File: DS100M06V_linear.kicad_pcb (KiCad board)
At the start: 4 copper layers, 110 x 52 mm, 108 parts, among them J1 wire2board, J10 BNC_panel_mount, J11 wire2board, J2 Wire2Board, J3 wire2board, J4 wire2board, J5 Wire2Board, J6 Wire2Board, J7 Wire2Board, J8 red_safety_4mm_connector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

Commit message: Back to linear.
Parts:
- removed L2, L3: 4.7u, Inductor_SMD:L_Bourns_SRN6045TA
- added C3: 1u, Resistor_SMD:R_0603_1608Metric_Pad0.98x0.95mm_HandSolder, F.Cu at (170.7, 111.0)
- added PS1: IA0509S, Converter_DCDC:Converter_DCDC_XP_POWER-IAxxxxS_THT, F.Cu at (192.9, 125.8)
- added U3: L7905, Package_TO_SOT_THT:TO-220-3_Horizontal_TabDown, F.Cu at (175.2, 111.9)
- SW1: footprint Button_Switch_THT:SW_CuK_JS202011CQN_DPDT_Straight -> Button_Switch_THT:SW_CK_JS202011CQN_DPDT_Straight
- U6: value TEA1-0505 -> L7805; footprint Converter_DCDC:Converter_DCDC_TRACO_TEA1-xxxx_THT -> Package_TO_SOT_THT:TO-220-3_Horizontal_TabDown
- moved RV5 52.7 mm to (128.8, 146.8), turned to 0 degrees
- moved Q2 48.1 mm to (144.3, 143.5), turned to 180 degrees
- moved U5 45.7 mm to (143.7, 139.6)
- moved C12 45.3 mm to (93.8, 114.5), turned to 180 degrees
- moved R29 45.2 mm to (139.4, 140.7)
- moved C13 43.9 mm to (99.0, 114.5), turned to 180 degrees
- moved R14 43.5 mm to (120.9, 109.5), turned to 90 degrees
- moved C14 42.7 mm to (104.2, 114.5), turned to 180 degrees
- moved D5 41.8 mm to (124.7, 109.2), turned to 90 degrees
- moved C15 41.5 mm to (109.4, 114.5), turned to 180 degrees
- moved U2 40.8 mm to (153.7, 144.4), turned to 180 degrees
- moved D4 40.1 mm to (122.7, 109.2), turned to 90 degrees
- moved C2 39.8 mm to (146.8, 139.7), turned to 90 degrees
- moved C8 35.8 mm to (122.6, 113.0)
- moved R30 35.7 mm to (148.4, 139.7), turned to -90 degrees
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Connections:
- C1 pad 2: 0 -> Earth
- C16 pad 1: 0 -> Earth
- C17 pad 1: 0 -> Earth
- C17 pad 2: Net-(U6-+Vin) -> Net-(PS1-+Vin)
- C2 pad 2: 0 -> Earth
- C28 pad 1: Net-(U6-+Vin) -> Net-(PS1-+Vin)
- C28 pad 2: 0 -> Earth
- C29 pad 1: Net-(U6--Vout) -> Net-(PS1--Vout)
- J5 pad 1: 0 -> Earth
- Q2 pad 1: (no net) -> unconnected-(Q2-D-Pad1)
- Q2 pad 2: (no net) -> Earth
- Q2 pad 3: (no net) -> Earth
- Q2 pad 6: (no net) -> -BAT
- Q2 pad 7: (no net) -> -BAT
- Q2 pad 8: (no net) -> unconnected-(Q2-D-Pad8)
- R25 pad 1: 0 -> Earth
- R26 pad 1: 0 -> Earth
- R27 pad 1: 0 -> Earth
- R28 pad 2: Net-(U6-+Vin) -> Net-(PS1-+Vin)
- U2 pad 3: 0 -> Earth
- U2 pad 9: 0 -> Earth
- U5 pad 6: 0 -> Earth
- U6 pad 1: 0 -> Net-(PS1-+Vout)
- U6 pad 2: Net-(U6-+Vin) -> 0
- U6 pad 3: Net-(U6--Vout) -> +5V
- U7 pad 2: 0 -> Earth
- U7 pad 5: Net-(U6-+Vin) -> Net-(PS1-+Vin)
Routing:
- net 0: track 80.0 -> 30.4 mm
- net (no net): track 41.0 -> 0.00 mm
- net +5V: track 61.1 -> 41.3 mm
- net Net-(C15-Pad1): track 23.4 -> 4.26 mm
- net Net-(C11-Pad1): track 28.0 -> 8.89 mm
- net Net-(U6-+Vin): track 12.0 -> 0.00 mm
- net -5V: track 25.7 -> 17.5 mm
- net Net-(R12-Pad1): track 4.90 -> 0.00 mm
- net Net-(R5-Pad1): track 4.42 -> 0.00 mm
- net Net-(C12-Pad1): track 0.00 -> 3.46 mm
- net Net-(C14-Pad1): track 0.00 -> 3.38 mm
- net Net-(C13-Pad1): track 0.00 -> 3.38 mm
- net Net-(U1B-+): track 9.59 -> 6.31 mm
- net Net-(U1A-+): track 10.1 -> 6.83 mm
- net IN-: track 6.09 -> 5.37 mm

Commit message: Ill flip ya for it.
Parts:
- added H5: WireFeedHole, MountingHole:MountingHole_2.2mm_M2_ISO7380, F.Cu at (94.0, 109.0)
- added H6: WireFeedHole, MountingHole:MountingHole_2.2mm_M2_ISO7380, F.Cu at (89.0, 112.0)
- added H7: WireFeedHole, MountingHole:MountingHole_2.2mm_M2_ISO7380, F.Cu at (93.0, 140.0)
- added H8: WireFeedHole, MountingHole:MountingHole_2.2mm_M2_ISO7380, F.Cu at (89.0, 137.0)
- J10, J8, PS1, RV1, RV2, RV3, RV4, RV5, RV6: moved to B.Cu
- J9: footprint DS100M06V_linear:black_safety_4mm_connector -> DS100M06V_linear:red_safety_4mm_connector; moved to B.Cu
- moved C28 8.33 mm to (192.3, 120.4)
- moved RV6 7.40 mm to (115.8, 102.5), turned to 180 degrees
- moved RV2 5.91 mm to (126.7, 126.0), turned to 0 degrees
- moved RV1 5.65 mm to (112.9, 147.0), turned to 180 degrees
- moved RV5 5.05 mm to (123.8, 146.9), turned to 180 degrees
- moved RV3 4.69 mm to (129.3, 101.9), turned to 180 degrees
- moved J10 3.22 mm to (196.9, 136.9)
- moved C10 3.00 mm to (104.2, 133.0)
- moved C11 3.00 mm to (109.4, 133.0)
- moved C39 3.00 mm to (93.7, 133.0)
- moved C9 3.00 mm to (99.0, 133.0)
- moved J3 3.00 mm to (89.5, 133.1)
- moved R1 3.00 mm to (99.0, 135.5)
- moved R2 3.00 mm to (104.2, 135.5)
- moved R3 3.00 mm to (109.4, 135.5)
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
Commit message: Veći prekidač.
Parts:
- SW1: footprint Button_Switch_THT:SW_CK_JS202011CQN_DPDT_Straight -> DS100M06V_linear:DPDT_bigger
- moved C17 5.90 mm to (166.0, 138.0)
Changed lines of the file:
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@@
 	(footprint "Resistor_SMD:R_0603_1608Metric_Pad0.98x0.95mm_HandSolder"
 		(layer "F.Cu")
-		(at 166.2 143.9 180)
+		(at 166 138 180)
 		(descr "Resistor SMD 0603 (1608 Metric), square (rectangular) end terminal, IPC_7351 nominal with elongated pad for handsoldering. (Body size source: IPC-SM-782 page 72, https://www.pcb-3d.com/wordpress/wp-content/uploads/ipc-sm-782a_amendment_1_and_2.pdf), generated with kicad-footprint-generator")
 		(tags "resistor handsolder")
@@
 		)
 	)
-	(footprint "Button_Switch_THT:SW_CK_JS202011CQN_DPDT_Straight"
+	(footprint "DS100M06V_linear:DPDT_bigger"
 		(layer "F.Cu")
 		(at 139 121.3575)
@@
 			)
 		)
-		(property "Footprint" "Button_Switch_THT:SW_CK_JS202011CQN_DPDT_Straight"
+		(property "Footprint" "DS100M06V_linear:DPDT_bigger"
 			(at 0 0 0)
 			(unlocked yes)
@@
 		)
 		(fp_line
-			(start -2.25 -0.95)
-			(end 7.25 -0.95)
+			(start -2.25 4.3)
+			(end -2.25 -0.95)
 			(stroke
 				(width 0.05)
@@
 		)
 		(fp_line
-			(start -2.25 4.25)
-			(end -2.25 -0.95)
+			(start -1.75 -1)
+			(end 10.7 -1)
 			(stroke
 				(width 0.05)
@@
 		)
 		(fp_line
-			(start 7.25 -0.95)
-			(end 7.25 4.25)
+			(start 10.7 -1)
+			(end 10.7 4.3)
 			(stroke
 				(width 0.05)
@@
 		)
 		(fp_line
-			(start 7.25 4.25)
-			(end -2.25 4.25)
+			(start 10.7 4.3)
+			(end -2.25 4.3)
 			(stroke
 				(width 0.05)
@@
 			)
 		)
-		(pad "1" thru_hole roundrect
-			(at 0 0)
-			(size 1.4 1.4)
-			(drill 0.9)
+		(pad "1" thru_hole oval
+			(at 0 0.1)
+			(size 2.7 1.5)
+			(drill oval 2.2 1)
 			(layers "*.Cu" "*.Mask")
 			(remove_unused_layers no)
-			(roundrect_rratio 0.1785714286)
 			(net 23 "Net-(SW1A-A)")
 			(pinfunction "A")
 			(pintype "passive")
 		)
-		(pad "2" thru_hole circle
-			(at 2.5 0)
-			(size 1.4 1.4)
-			(drill 0.9)
+		(pad "2" thru_hole oval
+			(at 4 0.1)
+			(size 2.7 1.5)
+			(drill oval 2.2 1)
 			(layers "*.Cu" "*.Mask")
 			(remove_unused_layers no)
@@
 			(pintype "passive")
 		)
-		(pad "3" thru_hole circle
-			(at 5 0)
-			(size 1.4 1.4)
-			(drill 0.9)
+		(pad "3" thru_hole oval
+			(at 8 0.1)
+			(size 2.7 1.5)
+			(drill oval 2.2 1)
 			(layers "*.Cu" "*.Mask")
 			(remove_unused_layers no)
@@
 			(pintype "passive")
 		)
-		(pad "4" thru_hole circle
-			(at 5 3.3)
-			(size 1.4 1.4)
-			(drill 0.9)
+		(pad "4" thru_hole oval
+			(at 8 3.2)
+			(size 2.7 1.5)
+			(drill oval 2.2 1)
 			(layers "*.Cu" "*.Mask")
 			(remove_unused_layers no)
@@
 			(pintype "passive")
 		)
-		(pad "5" thru_hole circle
-			(at 2.5 3.3)
-			(size 1.4 1.4)
-			(drill 0.9)
+		(pad "5" thru_hole oval
+			(at 4 3.2)
+			(size 2.7 1.5)
+			(drill oval 2.2 1)
 			(layers "*.Cu" "*.Mask")
 			(remove_unused_layers no)
@@
 			(pintype "passive")
 		)
-		(pad "6" thru_hole circle
-			(at 0 3.3)
-			(size 1.4 1.4)
-			(drill 0.9)
+		(pad "6" thru_hole oval
+			(at 0 3.2)
+			(size 2.7 1.5)
+			(drill oval 2.2 1)
 			(layers "*.Cu" "*.Mask")
 			(remove_unused_layers no)
@@
 			(pintype "passive")
 		)
-		(model "${KICAD8_3DMODEL_DIR}/Button_Switch_THT.3dshapes/SW_CK_JS202011CQN_DPDT_Straight.wrl"
+		(model "${DS100M06V}/DPDT Slide Switch.step"
 			(offset
-				(xyz 0 0 0)
+				(xyz -7 -1.6 8)
 			)
 			(scale
@@
 		(tags "cliff 4mm socket jack banana green")
 		(property "Reference" "J9"
-			(at 0 10.25 360)
+			(at 0 10.25 0)
 			(layer "B.SilkS")
 			(effects
@@
 		)
 		(property "Value" "black_safety_4mm_connector"
-			(at 0 -9.75 360)
+			(at 0 -9.75 0)
 			(layer "B.Fab")
 			(effects
@@
 		)
 		(fp_text user "${REFERENCE}"
-			(at 0 0 360)
+			(at 0 0 0)
 			(layer "B.Fab")
 			(effects
@@
 		(tags "cliff 4mm socket jack banana green")
 		(property "Reference" "J10"
-			(at 0 10.25 360)
+			(at 0 10.25 0)
 			(layer "B.SilkS")
 			(effects
@@
 		)
 		(property "Value" "BNC_panel_mount"
-			(at 0 -9.75 360)
+			(at 0 -9.75 0)
 			(layer "B.Fab")
 			(effects
@@
 		)
 		(fp_text user "${REFERENCE}"
-			(at 0 0 360)
+			(at 0 0 0)
 			(layer "B.Fab")
 			(effects
@@
 		(tags "cliff 4mm socket jack banana green")
 		(property "Reference" "J8"
-			(at 0 10.25 360)
+			(at 0 10.25 0)
 			(layer "B.SilkS")
 			(effects
@@
 		)
 		(property "Value" "red_safety_4mm_connector"
-			(at 0 -9.75 360)
+			(at 0 -9.75 0)
 			(layer "B.Fab")
 			(effects
@@
 		)
 		(fp_text user "${REFERENCE}"
-			(at 0 0 360)
+			(at 0 0 0)
 			(layer "B.Fab")
 			(effects

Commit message: Img tst
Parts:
- removed C16: 1n, Resistor_SMD:R_0603_1608Metric_Pad0.98x0.95mm_HandSolder
- removed RV3: 100, Potentiometer_THT:Potentiometer_Bourns_3296W_Vertical
- added C19: 1u, Resistor_SMD:R_0603_1608Metric_Pad0.98x0.95mm_HandSolder, F.Cu at (116.5, 120.2)
- added C33: 100n, Resistor_SMD:R_0603_1608Metric_Pad0.98x0.95mm_HandSolder, F.Cu at (116.5, 118.7)
- added C34: 1n, Resistor_SMD:R_0603_1608Metric_Pad0.98x0.95mm_HandSolder, F.Cu at (116.5, 117.2)
- added C36: 470u, Capacitor_THT:CP_Radial_D8.0mm_P3.50mm, B.Cu at (166.7, 134.5)
- added C4: 100n, Resistor_SMD:R_0603_1608Metric_Pad0.98x0.95mm_HandSolder, F.Cu at (145.4, 129.2)
- added C40: 470u, Capacitor_THT:CP_Radial_D8.0mm_P3.50mm, B.Cu at (168.6, 143.3)
- added C41: 10u, Resistor_SMD:R_1206_3216Metric_Pad1.30x1.75mm_HandSolder, F.Cu at (161.8, 146.8)
- added C42: 10u, Resistor_SMD:R_1206_3216Metric_Pad1.30x1.75mm_HandSolder, F.Cu at (161.8, 144.5)
- added C43: 10u, Resistor_SMD:R_1206_3216Metric_Pad1.30x1.75mm_HandSolder, F.Cu at (153.7, 145.8)
- added L2: 4.7u, Inductor_THT:L_Radial_D7.5mm_P3.50mm_Fastron_07P, B.Cu at (159.2, 139.8)
- added SW2: SW_DPDT_x2, DS100M06V_linear:DPDT_bigger, F.Cu at (136.5, 134.4)
- C17, C26: value 1n -> 1u
- C18, C21: value 1u -> 100n
- C20: value 1n -> 470u; footprint Resistor_SMD:R_0603_1608Metric_Pad0.98x0.95mm_HandSolder -> Capacitor_THT:CP_Radial_D8.0mm_P3.50mm; moved to B.Cu
- C35, C37: value 1u -> 1n
- moved C7 52.3 mm to (112.7, 133.0), turned to 90 degrees
- moved C6 51.7 mm to (115.9, 133.0), turned to 90 degrees
- moved C5 50.1 mm to (115.9, 114.7)
- moved TP3 37.6 mm to (166.7, 131.3)
- moved C20 36.3 mm to (166.6, 113.9), turned to -90 degrees
- moved J5 33.2 mm to (131.9, 146.0), turned to -90 degrees
- moved R23 29.2 mm to (114.0, 118.1), turned to -90 degrees
- moved TP4 28.4 mm to (166.5, 110.4)
- moved J2 26.4 mm to (135.7, 146.0), turned to -90 degrees
- moved R24 24.0 mm to (142.4, 122.0), turned to 0 degrees
- moved C3 23.2 mm to (169.6, 134.2), turned to -90 degrees
- moved C27 22.2 mm to (126.3, 125.4), turned to 180 degrees
- moved J10 21.8 mm to (190.9, 115.9)
- moved C25 20.8 mm to (148.8, 121.0)
- moved RV4 19.2 mm to (148.4, 125.8), turned to 0 degrees
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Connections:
- C20 pad 1: 0 -> -5V
- C20 pad 2: +5V -> 0
- L1 pad 1: +BAT -> Net-(SW2A-B)
- RV2 pad 1: 0 -> Net-(R12-Pad1)
- TP3 pad 1: -5V -> +5V
- U7 pad 3: +BAT -> Net-(SW2A-B)
- U7 pad 6: +BAT -> Net-(SW2A-B)
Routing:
- net +5V: track 41.4 -> 5.34 mm
- net 0: track 30.4 -> 6.45 mm
- net -5V: track 17.3 -> 1.48 mm
- net Net-(C15-Pad1): track 4.26 -> 17.2 mm
- net Net-(SW1B-A): track 7.35 -> 14.8 mm
- net Net-(C32-Pad2): track 6.70 -> 0.00 mm
- net Net-(SW1B-C): track 11.7 -> 5.05 mm
- net Net-(U1A-+): track 6.83 -> 13.4 mm
- net Net-(D4-K): track 0.00 -> 5.57 mm
- net Net-(J1-Pin_1): track 4.73 -> 0.00 mm
- net Net-(U4--): track 12.8 -> 8.67 mm
- net Net-(C11-Pad1): track 8.89 -> 12.3 mm
- net Net-(SW1A-C): track 11.0 -> 14.3 mm
- net Net-(U1B-+): track 6.31 -> 9.43 mm
- net Net-(SW1A-B): track 12.9 -> 14.8 mm
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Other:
- board text removed: "+"
- board text removed: "-"
- board text removed: "-5V"
- board text removed: "G"

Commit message: Layout skoro gotov.
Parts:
- C27: value 1n -> 1u
- moved J6 15.2 mm to (130.8, 138.9)
- moved C43 10.7 mm to (155.6, 135.3), turned to 0 degrees
- moved R29 7.43 mm to (136.8, 144.7)
- moved D7 3.63 mm to (120.3, 123.0), turned to 0 degrees
- moved H2 3.40 mm to (180.0, 104.9)
- moved H4 3.40 mm to (180.0, 144.9)
- moved J5 2.64 mm to (134.3, 147.1)
- moved C20 2.60 mm to (166.7, 116.5)
- moved PS1 2.45 mm to (189.6, 125.4)
- moved C18 2.43 mm to (123.9, 123.6)
- moved C27 2.43 mm to (123.9, 125.0)
- moved C35 2.43 mm to (123.9, 122.1)
- moved TP4 2.41 mm to (166.7, 112.8)
- moved J2 1.98 mm to (137.3, 147.1)
- moved TP1 1.82 mm to (115.7, 127.9)
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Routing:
- net +5V: track 5.34 -> 158.0 mm, vias 0 -> 6
- net -5V: track 1.48 -> 132.8 mm, vias 0 -> 6
- net Net-(PS1-+Vin): track 0.00 -> 53.0 mm
- net 0: track 6.45 -> 52.1 mm, vias 0 -> 22
- net Net-(SW2A-B): track 0.00 -> 41.0 mm, vias 0 -> 1
- net +BAT: track 0.00 -> 20.8 mm, vias 0 -> 1
- net Earth: track 0.00 -> 19.0 mm, vias 0 -> 13
- net Net-(PS1--Vout): track 0.00 -> 18.6 mm
- net Net-(PS1-+Vout): track 0.00 -> 12.0 mm
- net Net-(U2-CE): track 0.00 -> 11.5 mm, vias 0 -> 2
- net Net-(C4-Pad2): track 0.00 -> 9.94 mm
- net -BAT: track 0.00 -> 7.27 mm
- net Net-(U5-CS): track 0.00 -> 6.07 mm
- net Net-(U5-VCC): track 0.00 -> 6.04 mm
- net +VBUS: track 0.00 -> 5.99 mm
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- added copper zone on In1.Cu, net 0
- added copper zone on In1.Cu, net Earth

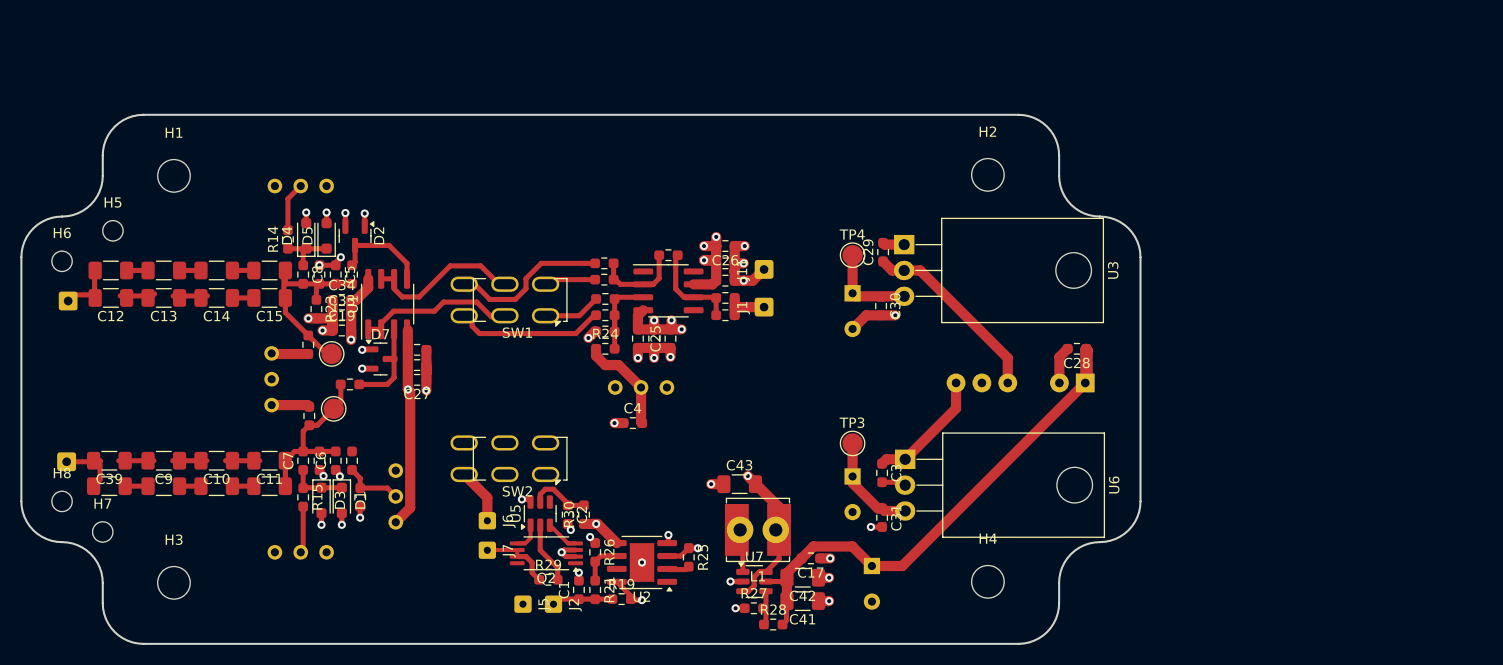
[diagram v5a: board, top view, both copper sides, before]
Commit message: Added PCB spacers.
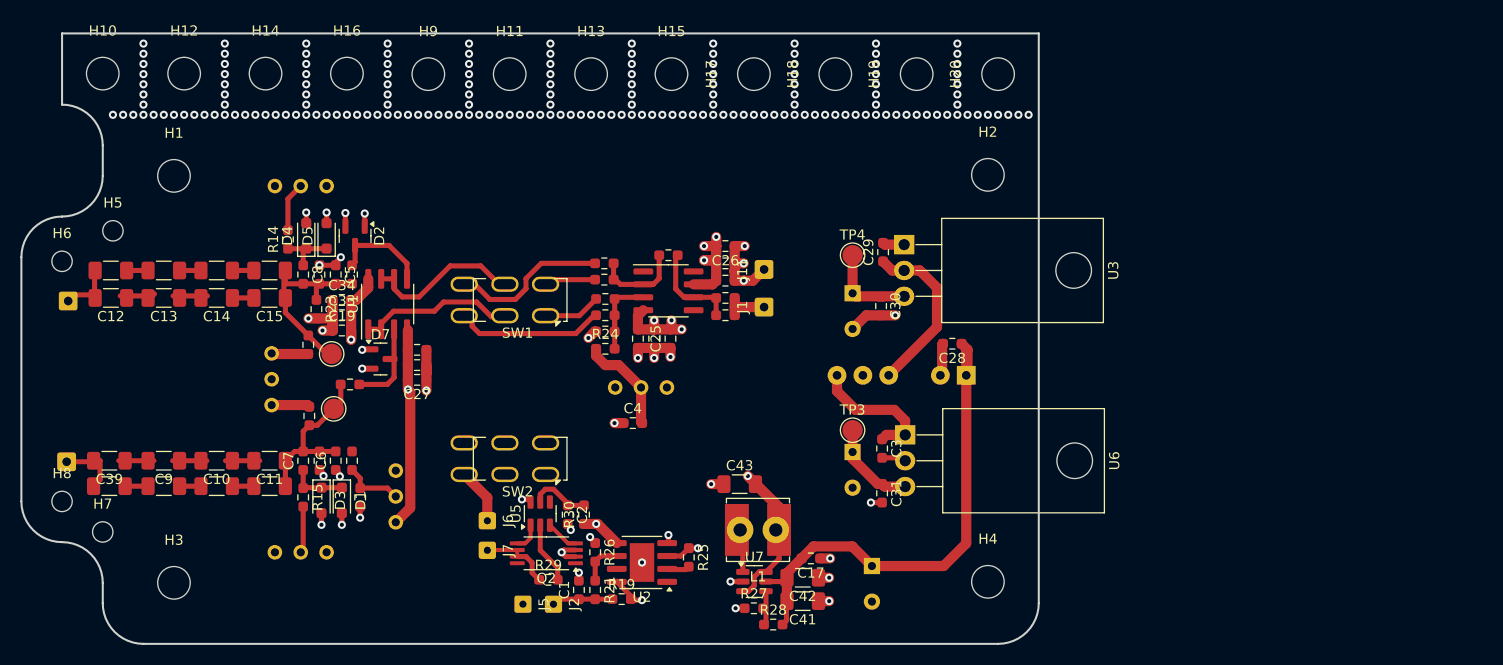
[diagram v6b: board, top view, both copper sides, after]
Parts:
- added H10: MountingHole, MountingHole:MountingHole_3.2mm_M3, F.Cu at (93.0, 95.0)
- added H11: MountingHole, MountingHole:MountingHole_3.2mm_M3, F.Cu at (133.0, 95.0)
- added H12: MountingHole, MountingHole:MountingHole_3.2mm_M3, F.Cu at (101.0, 95.0)
- added H13: MountingHole, MountingHole:MountingHole_3.2mm_M3, F.Cu at (141.0, 95.0)
- added H14: MountingHole, MountingHole:MountingHole_3.2mm_M3, F.Cu at (109.0, 95.0)
- added H15: MountingHole, MountingHole:MountingHole_3.2mm_M3, F.Cu at (148.9, 95.0)
- added H16: MountingHole, MountingHole:MountingHole_3.2mm_M3, F.Cu at (117.0, 95.0)
- added H17: MountingHole, MountingHole:MountingHole_3.2mm_M3, F.Cu at (157.0, 95.0)
- added H18: MountingHole, MountingHole:MountingHole_3.2mm_M3, F.Cu at (165.0, 95.0)
- added H19: MountingHole, MountingHole:MountingHole_3.2mm_M3, F.Cu at (173.0, 95.0)
- added H20: MountingHole, MountingHole:MountingHole_3.2mm_M3, F.Cu at (181.0, 95.0)
- added H9: MountingHole, MountingHole:MountingHole_3.2mm_M3, F.Cu at (125.0, 95.0)
- moved C28 12.3 mm to (176.5, 121.5)
- moved PS1 11.7 mm to (177.9, 124.6)
- moved C31 2.40 mm to (169.6, 136.2)
- moved C36 2.40 mm to (166.7, 132.1)
- moved U6 2.40 mm to (171.9, 130.5)
- moved C3 2.40 mm to (169.6, 131.8)
- moved TP3 1.30 mm to (166.7, 130.0)
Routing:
- net Net-(PS1-+Vin): track 53.0 -> 50.2 mm
- net Net-(PS1--Vout): track 18.6 -> 16.9 mm
- net Net-(PS1-+Vout): track 12.0 -> 13.3 mm
- net +5V: track 158.0 -> 156.9 mm
- net 0: vias 22 -> 190
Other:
- board size 110 x 52 mm -> 100 x 60 mm
